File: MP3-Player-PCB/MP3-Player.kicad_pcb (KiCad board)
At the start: 4 copper layers, 50 x 50 mm, 113 parts, among them J101 Conn_ARM_SWD_TagConnect_TC2030, J201 Conn_01x02_Socket, J202 USB_C_Receptacle_USB2.0_16P, J301 Micro_SD_Card_Det1, Q301 AO3401A, Q302 2N7002H, Q303 AO3401A, Q304 AO3401A, Q305 2N7002H, SW301 1-1825910-4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

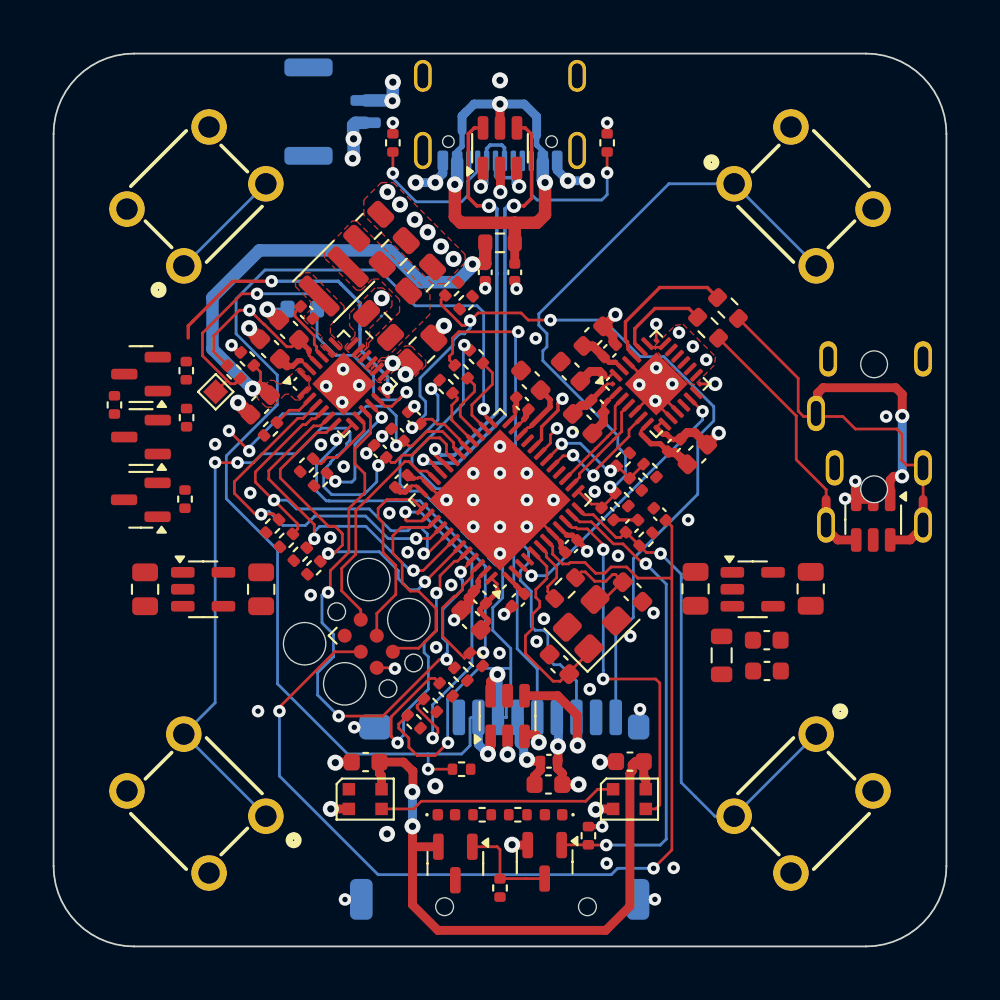
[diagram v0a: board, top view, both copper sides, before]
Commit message: Routed out shipping mode exit logic circuitry
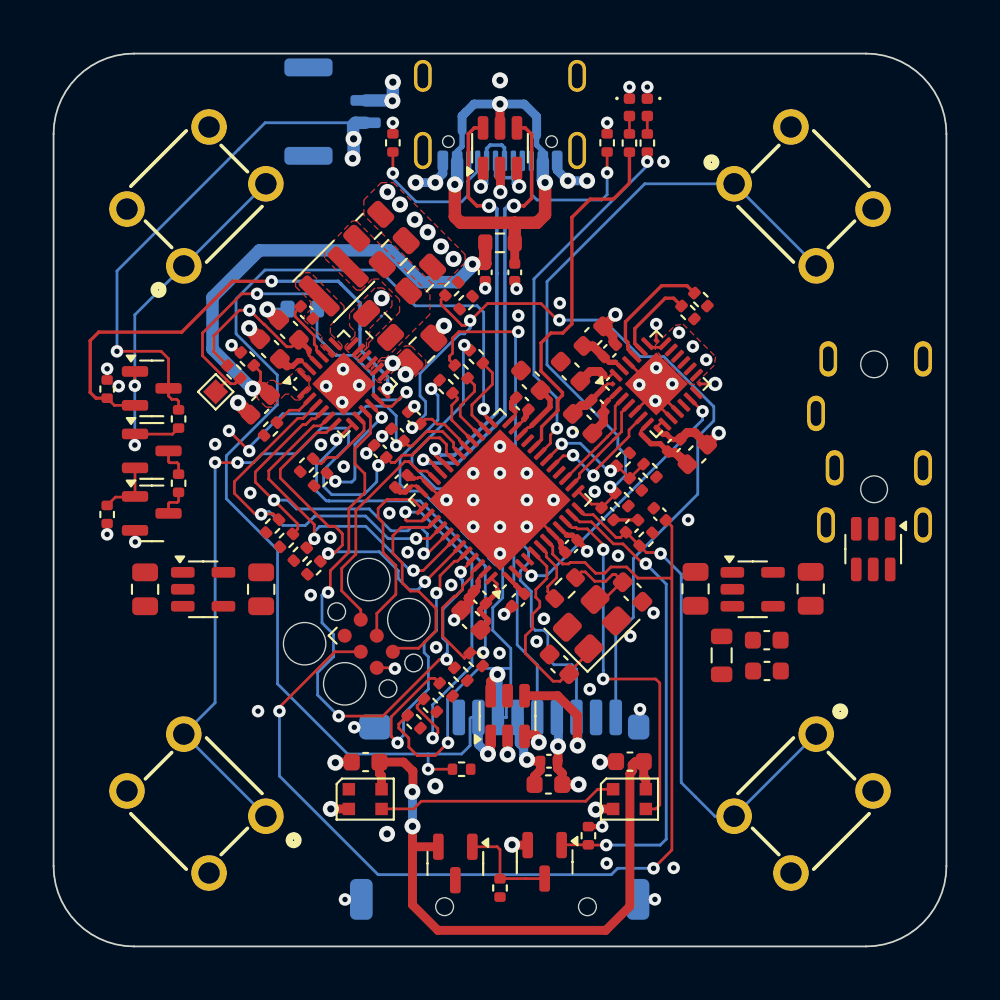
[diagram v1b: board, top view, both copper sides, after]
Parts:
- R401, R402: footprint Resistor_SMD:R_0603_1608Metric -> Resistor_SMD:R_0402_1005Metric
- moved D102 40.9 mm to (132.2, 103.0), turned to -90 degrees
- moved D101 40.0 mm to (133.2, 103.0), turned to -90 degrees
- moved R104 38.5 mm to (132.2, 105.0), turned to 90 degrees
- moved R103 38.3 mm to (133.2, 105.0), turned to 90 degrees
- moved R314 9.19 mm to (103.0, 125.8), turned to -90 degrees
- moved Q305 7.82 mm to (105.5, 125.8), turned to 0 degrees
- moved R313 7.55 mm to (103.0, 118.8), turned to 90 degrees
- moved Q303 6.27 mm to (105.5, 118.8), turned to 0 degrees
- moved R315 5.67 mm to (107.0, 124.1), turned to -90 degrees
- moved U403 1.65 mm to (145.9, 127.8)
- moved R402 1.59 mm to (136.2, 113.8)
- moved R401 1.41 mm to (135.5, 114.5)
- moved Q304 0.98 mm to (105.5, 122.2), turned to 0 degrees
- moved R309 0.45 mm to (107.0, 120.5)
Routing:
- net +VBAT: track 2.66 -> 30.8 mm, vias 4 -> 5
- net /DAC/DAC_AUDIO_RIGHT: track 21.0 -> 0.00 mm
- net /MCU/BAT_STATUS: track 1.79 -> 20.4 mm, vias 1 -> 2
- net /MCU/BAT_CHARGING_STATUS: track 3.37 -> 20.9 mm, vias 1 -> 0
- net /Peripherals/BUTTON4_GATE: track 6.50 -> 21.7 mm, vias 0 -> 2
- net /DAC/DAC_AUDIO_LEFT: track 15.1 -> 0.00 mm
- net AUDIO_JACK_DET: track 32.6 -> 20.3 mm, vias 4 -> 2
- net BAT_QON: track 17.6 -> 28.5 mm
- net /Peripherals/BUTTON4_ST_GATE: track 0.00 -> 3.38 mm
- net +3.3V: track 18.9 -> 20.8 mm
- net BUTTON_4: track 17.7 -> 19.4 mm
- net /DAC/DAC_PIN_R: track 8.34 -> 7.02 mm
- net /MCU/BAT_STATUS_LED_RES: track 0.00 -> 1.00 mm
- net /MCU/BAT_CHARGING_LED_RES: track 0.00 -> 1.00 mm
- net /DAC/DAC_PIN_L: track 5.54 -> 4.85 mm
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
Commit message: Finished routing more miscellaneous signals
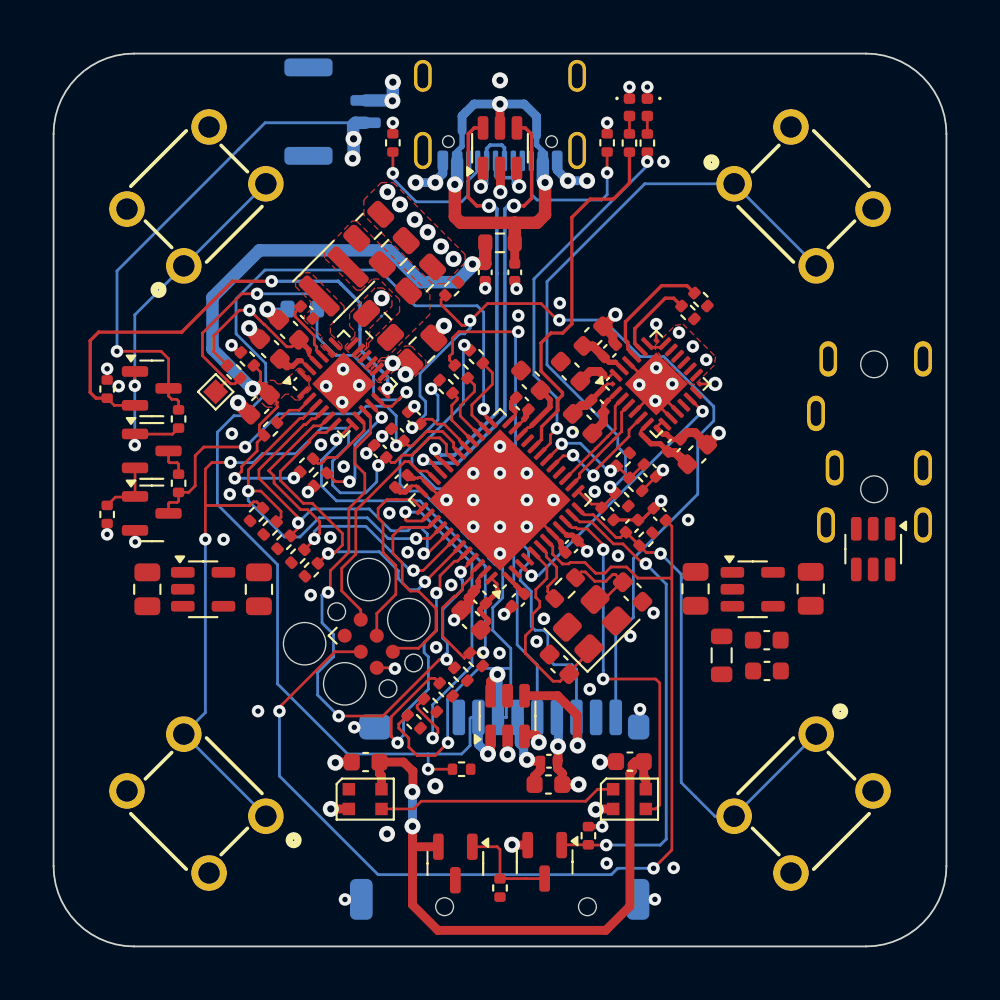
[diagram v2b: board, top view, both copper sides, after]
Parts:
- moved R308 16.7 mm to (111.4, 125.8), turned to 45 degrees
- moved C112 1.11 mm to (133.4, 123.3)
- moved R216 1.11 mm to (132.6, 124.1)
- moved R209 0.17 mm to (112.1, 126.6)
- moved R210 0.17 mm to (112.9, 127.4)
- moved R211 0.17 mm to (114.4, 128.9)
- moved R212 0.17 mm to (113.7, 128.1)
- moved C216 0.12 mm to (105.2, 130.0)
- moved C217 0.12 mm to (111.5, 130.0)
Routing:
- net +VUSB_FILT: track 27.8 -> 37.7 mm, vias 2 -> 4
- net BUTTON_4: track 19.4 -> 23.6 mm, vias 3 -> 2
- net GND: track 74.0 -> 77.9 mm, vias 104 -> 108
- net BUTTON_3: track 44.8 -> 47.5 mm
- net BAT_NPG: track 21.5 -> 23.0 mm
- net BAT_STAT: track 22.3 -> 21.0 mm
- net BAT_SCL: track 20.2 -> 20.9 mm
- net BAT_INT: track 28.5 -> 27.9 mm

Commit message: Replaced THT buttons with SMT
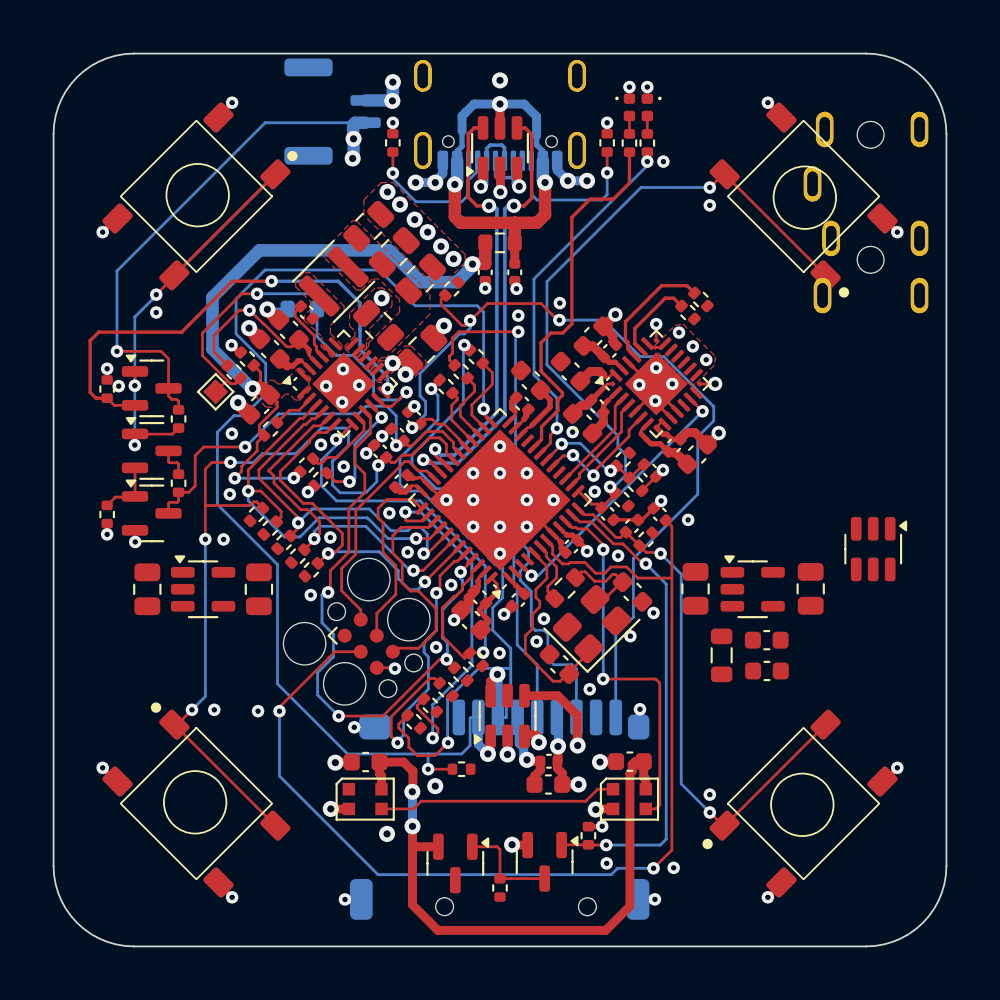
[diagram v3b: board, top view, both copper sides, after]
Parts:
- SW301, SW302, SW303, SW304: value 1-1825910-4 -> ZX-QC66-10.0TP; footprint MP3-Player_Footprint_Libraries:1-1825910-4 -> MP3-Player_Footprint_Libraries:ZX-QC66
- moved U402 12.9 mm to (145.5, 108.9)
- turned SW301 to 45 degrees
- turned SW302 to 135 degrees
- turned SW303 to -45 degrees
- turned SW304 to -135 degrees
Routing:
- net GND: track 77.9 -> 87.0 mm, vias 108 -> 120
- net /Peripherals/BUTTON4_GATE: track 21.7 -> 28.9 mm, vias 2 -> 3
- net BUTTON_3: track 47.5 -> 48.8 mm, vias 3 -> 4
- net BUTTON_1: track 29.5 -> 30.7 mm, vias 1 -> 2
- net BUTTON_2: track 36.5 -> 37.6 mm, vias 1 -> 2

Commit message: Finished Audio Jack routing
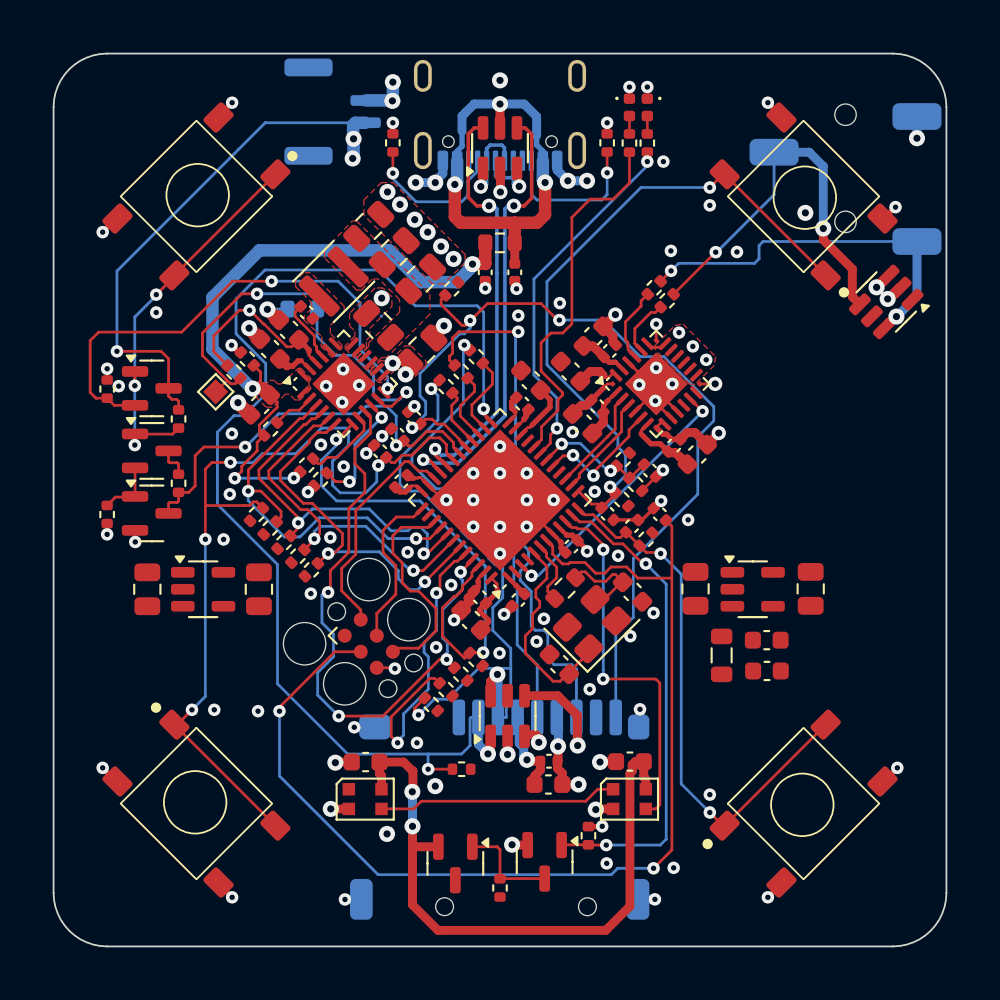
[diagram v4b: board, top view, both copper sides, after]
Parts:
- removed R406: 56k, Resistor_SMD:R_0402_1005Metric
- removed U402: ST-0322D00-071-1A2H, MP3-Player_Footprint_Libraries:ST-0322D00-071-1A2H
- added J402: PJ-320B, MP3-Player_Footprint_Libraries:PJ-320B, B.Cu at (144.3, 107.0)
- moved U403 13.9 mm to (146.6, 113.9), turned to -135 degrees
- moved R402 2.70 mm to (133.6, 113.1), turned to 45 degrees
- moved R302 1.36 mm to (121.2, 136.4)
- moved R401 1.34 mm to (134.4, 113.8), turned to 45 degrees
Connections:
- U101 pad 38: AUDIO_JACK_DET -> unconnected-(U101-PA15-Pad38)
- U403 pad 1: AUDIO_JACK_DET -> unconnected-(U403-D1+-Pad1)
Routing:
- net /DAC/DAC_AUDIO_LEFT: track 0.00 -> 22.0 mm, vias 0 -> 2
- net /DAC/DAC_AUDIO_RIGHT: track 0.00 -> 21.4 mm, vias 0 -> 2
- net AUDIO_JACK_DET: track 20.3 -> 0.00 mm, vias 2 -> 0
- net /Peripherals/BUTTON4_GATE: track 28.9 -> 22.4 mm
- net /Peripherals/SD_CARD_MOSI_PIN: track 40.1 -> 36.0 mm
- net GND: track 87.0 -> 90.0 mm, vias 120 -> 126
- net /DAC/DAC_PIN_R: track 7.02 -> 4.22 mm
- net /DAC/DAC_PIN_L: track 4.85 -> 3.30 mm
- net /MCU/SWD_SWCLK: track 10.9 -> 9.32 mm
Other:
- outline, holes or cut-outs redrawn

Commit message: Finished routinggit status! DRC needed
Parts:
- moved C215 1.35 mm to (143.8, 130.0)
- moved U203 1.35 mm to (140.5, 130.0)
- moved C214 1.30 mm to (137.2, 130.0)
- moved C212 0.93 mm to (140.0, 135.5)
- moved FB201 0.80 mm to (137.5, 134.5)
- moved C216 0.75 mm to (104.5, 130.0)
- moved C213 0.65 mm to (140.0, 133.5)
- moved U204 0.62 mm to (107.8, 130.0)
- moved C217 0.50 mm to (111.0, 130.0)
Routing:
- net +3.3V: track 20.8 -> 230.7 mm, vias 2 -> 11
- net +VSYS: track 0.00 -> 122.9 mm, vias 0 -> 6
- net +3.3VA: track 2.76 -> 31.7 mm, vias 0 -> 2
- net /MCU/NRST: track 61.6 -> 80.8 mm, vias 2 -> 3
- net GND: track 90.0 -> 106.0 mm, vias 126 -> 149
- net +VSYS_FILT: track 0.00 -> 11.4 mm
- net +VSYS_LED: track 36.3 -> 30.7 mm, vias 2 -> 4
- net /MCU/BOOT: track 17.8 -> 14.2 mm
- net SD_CARD_NCD: track 50.6 -> 51.8 mm
- net /Peripherals/SD_CARD_MOSI_PIN: track 36.0 -> 37.0 mm
- net /Peripherals/SD_CARD_MISO_PIN: track 36.6 -> 37.2 mm
- added copper zone on F.Cu, net +3.3V
- added copper zone on F.Cu, net +3.3VA
- added copper zone on F.Cu, net +VSYS_FILT

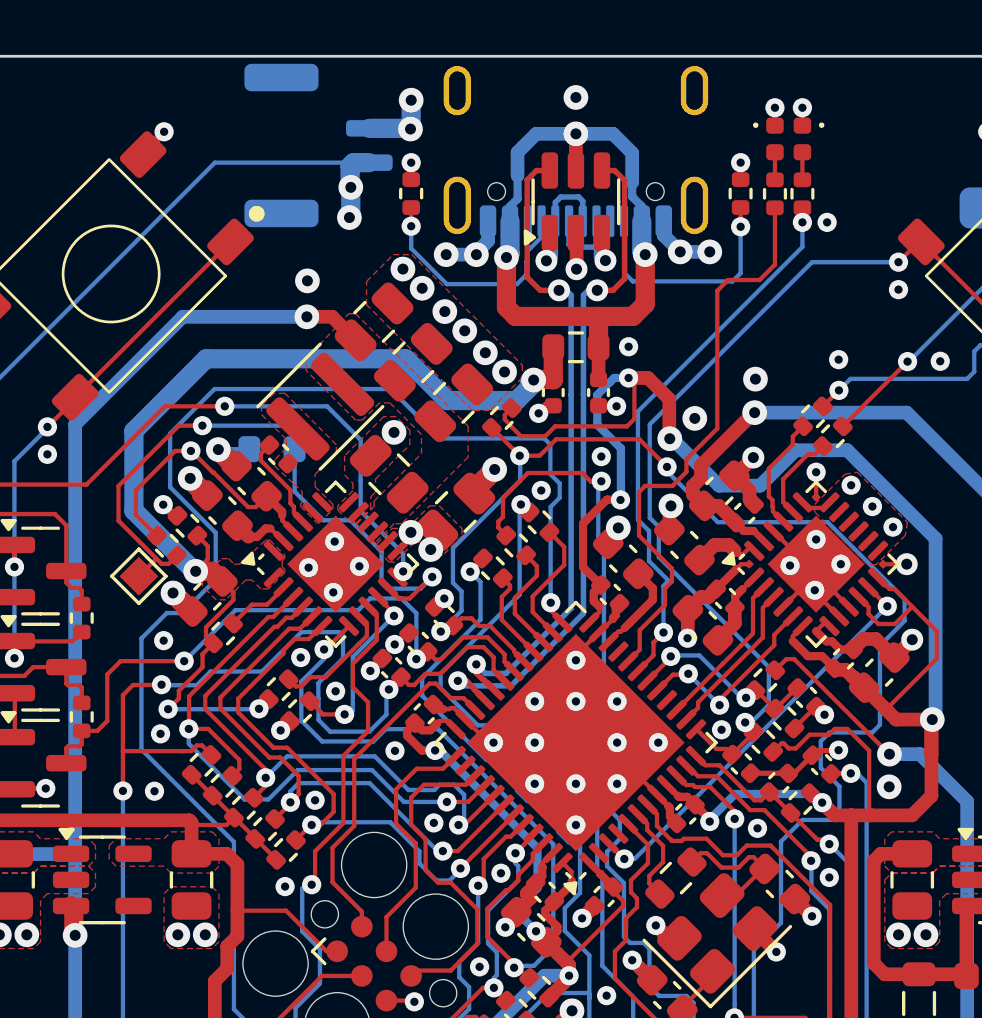
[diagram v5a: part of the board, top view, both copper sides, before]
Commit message: Fixed all DRC errors
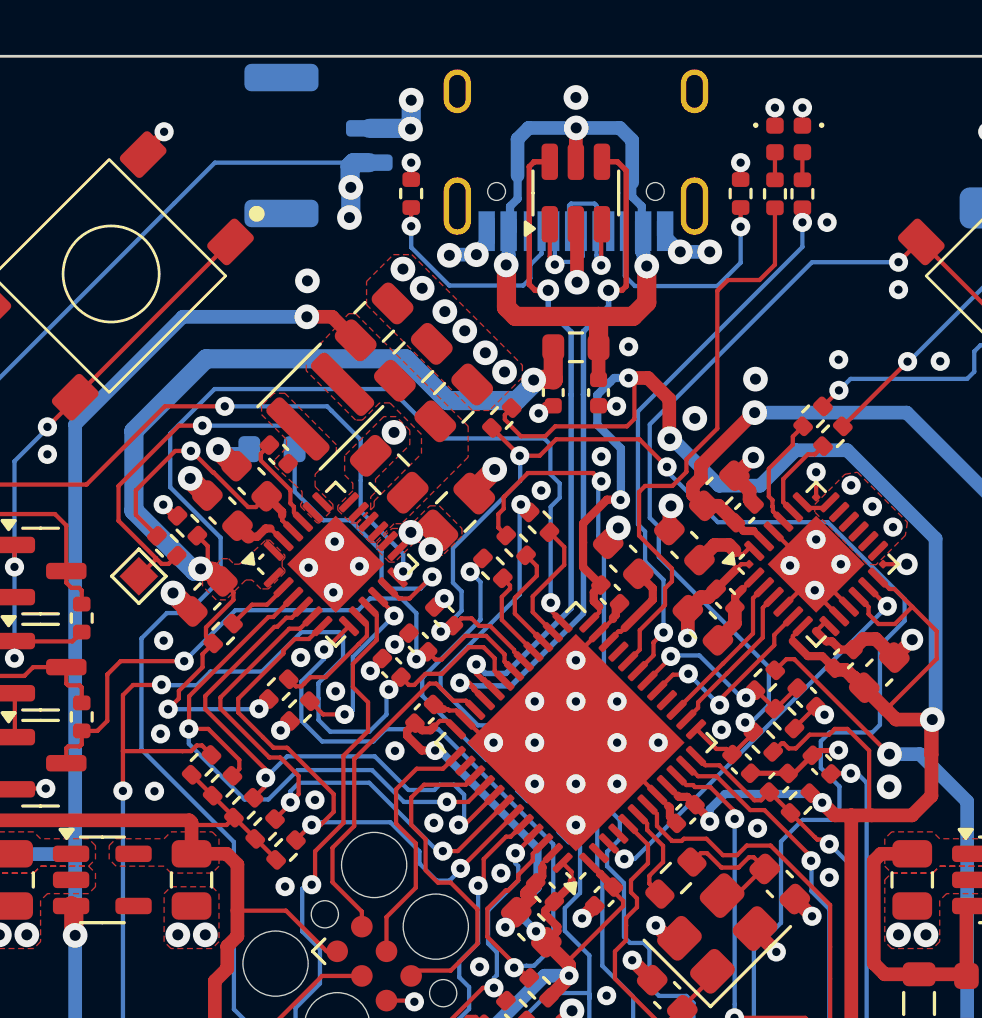
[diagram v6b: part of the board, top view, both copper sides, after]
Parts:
- J202: footprint Connector_USB:USB_C_Receptacle_GCT_USB4105-xx-A_16P_TopMnt_Horizontal -> Connector_USB:USB_C_Receptacle_HRO_TYPE-C-31-M-12
- moved U202 0.32 mm to (125.0, 105.0)
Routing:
- net +VUSB: track 25.3 -> 26.0 mm
- net GND: track 106.0 -> 106.5 mm
